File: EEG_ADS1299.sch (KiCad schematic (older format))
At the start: 68 parts, among them IC1 ADS1299, P1 CONN_2, P2 CONN_2, P3 CONN_01X06, U1 TPS61221, U2 TPS61222, U3 NRF528XX-QFAA, U4 MPU-9250, U5 INA828, U6 INA828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

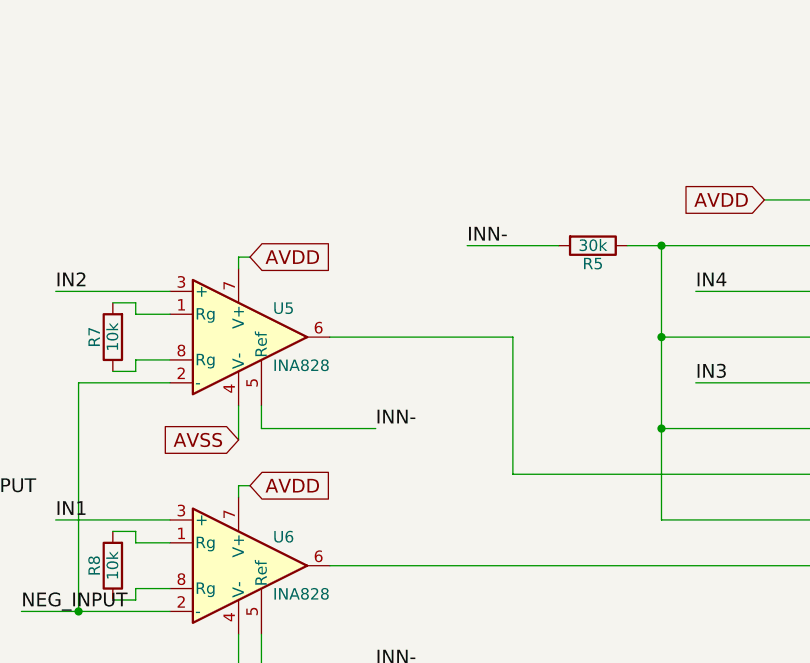
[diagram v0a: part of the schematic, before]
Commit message: (#1) - Added single capacitor on amp inputs. (C37)
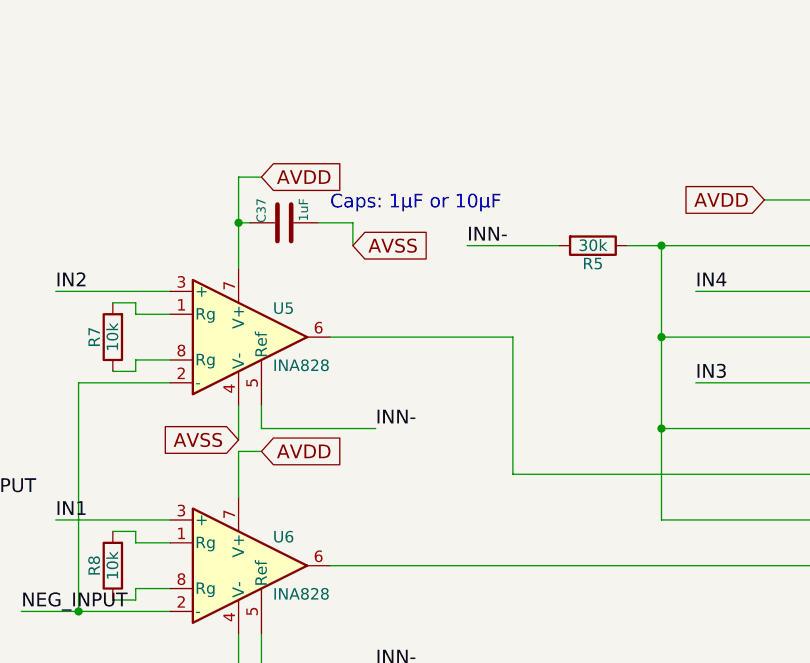
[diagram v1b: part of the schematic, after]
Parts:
- added C37: 1uF, Capacitors_SMD:C_0402, symbol C
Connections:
- wire segments 310 -> 313
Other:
- note added: "Caps: 1µF or 10µF"
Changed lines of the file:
@@
 Text GLabel 10600 11950 0    60   Input ~ 0
 AVSS
-Text GLabel 10650 11100 2    60   Input ~ 0
+Text GLabel 10700 10950 2    60   Input ~ 0
 AVDD
-Text GLabel 10650 10100 2    60   Input ~ 0
+Text GLabel 10700 9750 2    60   Input ~ 0
 AVDD
 $Comp
@@
 	10050 10600 10150 10600
 Wire Wire Line
-	10600 10100 10650 10100
-Wire Wire Line
-	10600 10150 10600 10100
-Wire Wire Line
-	10600 11100 10650 11100
-Wire Wire Line
-	10600 11100 10600 11150
+	10600 9750 10600 10150
+Wire Wire Line
+	10600 10950 10600 11150
 Wire Wire Line
 	10700 11900 11200 11900
@@
 Wire Wire Line
 	13850 10450 12450 10450
+$Comp
+L C C37
+U 1 1 5A28A53A
+P 10800 9950
+F 0 "C37" H 10800 10050 40  0000 L CNN
+F 1 "1uF" H 10806 9865 40  0000 L CNN
+F 2 "Capacitors_SMD:C_0402" H 10838 9800 30  0001 C CNN
+F 3 "~" H 10800 9950 60  0000 C CNN
+	1    10800 9950
+	0    -1   -1   0
+$EndComp
+Wire Wire Line
+	10600 9750 10700 9750
+Wire Wire Line
+	10600 9950 10650 9950
+Connection ~ 10600 9950
+Wire Wire Line
+	10950 9950 11100 9950
+Wire Wire Line
+	11100 9950 11100 10050
+Text GLabel 11100 10050 2    60   Input ~ 0
+AVSS
+Wire Wire Line
+	10600 10950 10700 10950
+Text Notes 11000 9900 0    60   ~ 0
+Caps: 1µF or 10µF
 $EndSCHEMATC

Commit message: Added TPS63001, TPS22941.
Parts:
- removed U1: TPS61221, TO_SOT_Packages_SMD:SOT-363_SC-70-6, symbol TPS61221
- added C38, C39: 10uF, Capacitors_SMD:C_0402, symbol C
- added C40: 1uF, Capacitors_SMD:C_0402, symbol C
- added R10, R9: 1M, Resistors_SMD:R_0402, symbol R
- added U1: TPS2294x, TO_SOT_Packages_SMD:SOT-353_SC-70-5, symbol TPS2294x
- added U7: TPS63001, Housings_DFN_QFN:DFN-10-1EP_3x3mm_Pitch0.5mm, symbol TPS63001
- L1: value 4.7µH -> 2.2µH
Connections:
- net labels added: AIN_BAT_DIV_VOLTAGE, IN1N, IN2N, IN3N, IN4N, LOAD_SW_CTRL, Vout
- net labels removed: BATT_ADC_AIN, BATT_VOLTAGE, GPIO_CTRL_PWR_ON, IN3-, IN4-
- wire segments 313 -> 348
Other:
- moved on the sheet: C1, C2, L1, P3

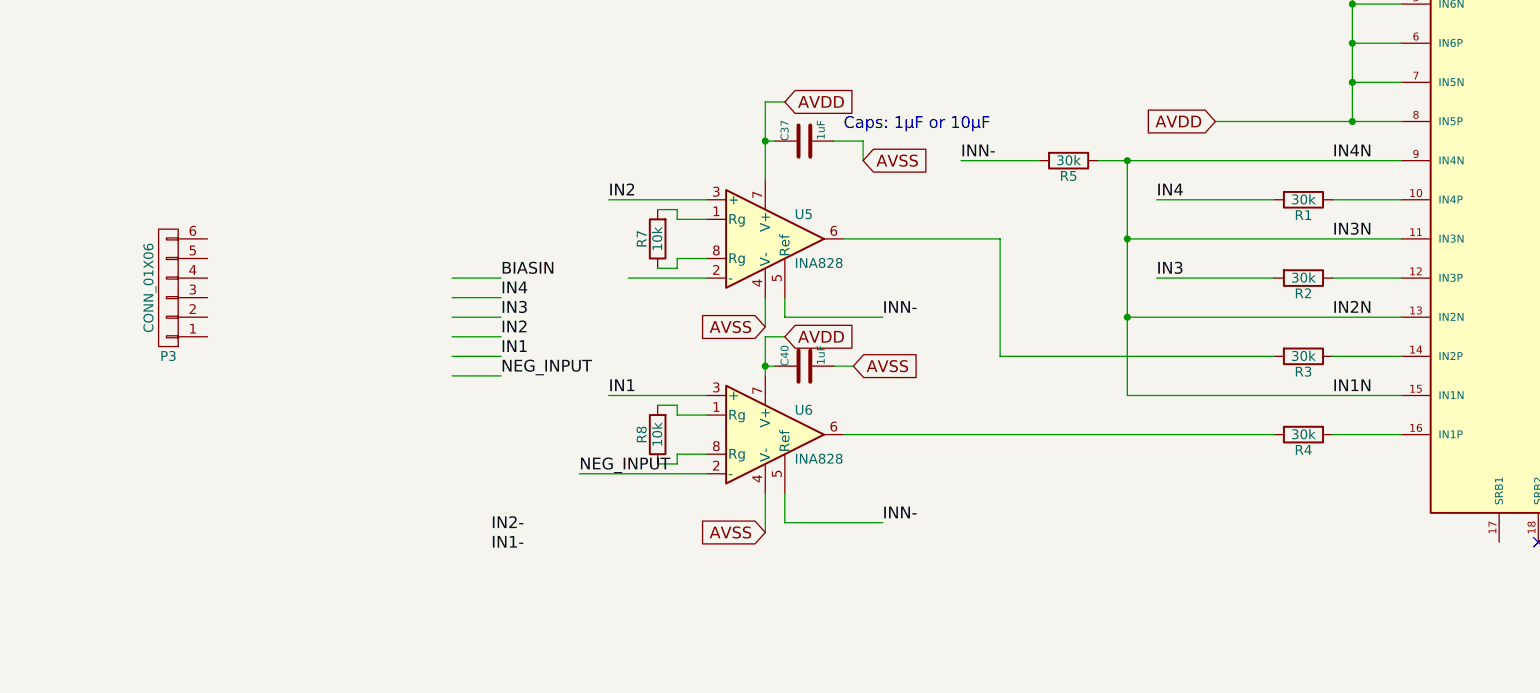
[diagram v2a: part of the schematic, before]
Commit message: Fixed design and separated channels 1 and 2 from 3 and 4, with 1 and 2 being the pre-amplified circuits.
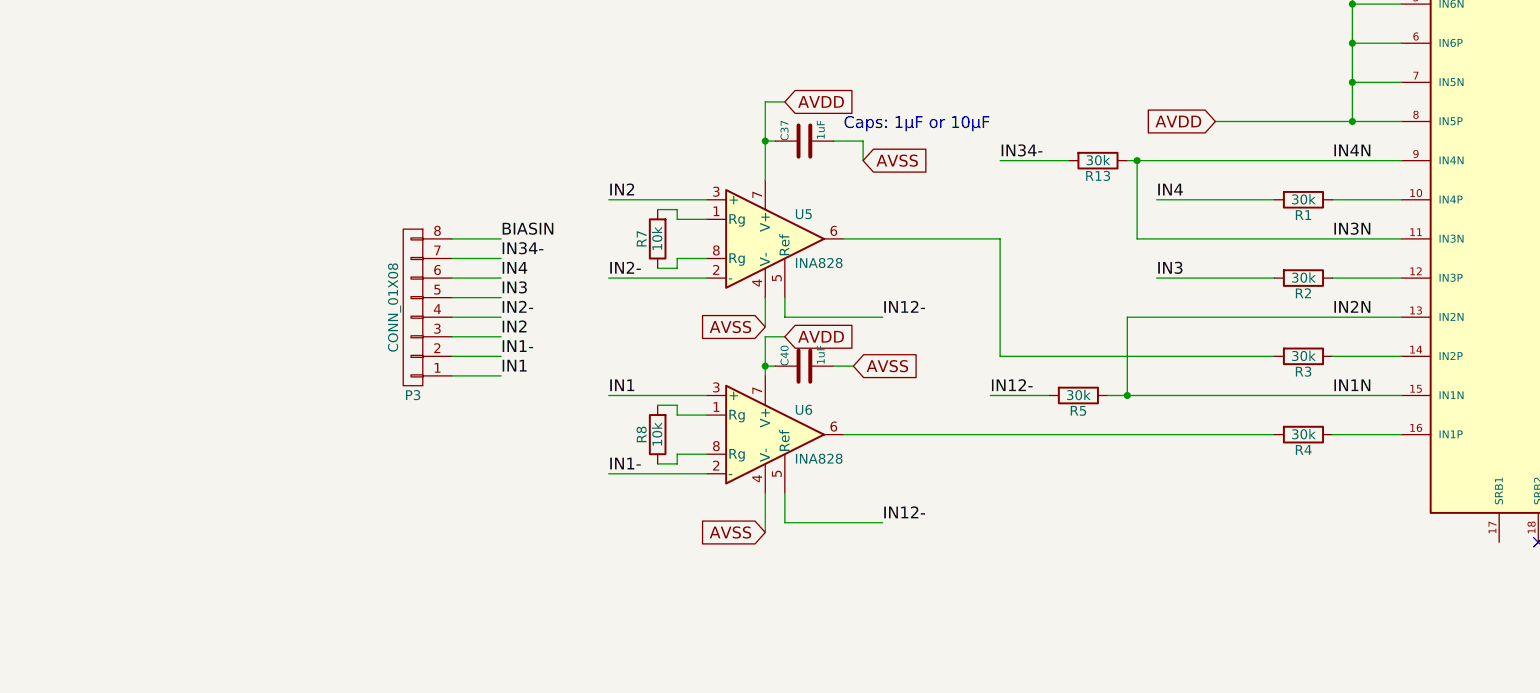
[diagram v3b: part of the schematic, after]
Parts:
- removed P3: CONN_01X06, Pin_Headers:Pin_Header_Straight_1x06_Pitch2.54mm, symbol CONN_01X06
- added P3: CONN_01X08, symbol CONN_01X08
- added R13: 30k, Resistors_SMD:R_0402, symbol R
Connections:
- net NEG_INPUT is gone; now on net IN1-: U6.2 (-)
- net BIASIN: now also P3.8 (P8)
- net IN1: now also P3.1 (P1)
- net IN1-: now also P3.2 (P2)
- net IN1N: no longer IC1.11 (IN3N), IC1.9 (IN4N)
- net IN2: now also P3.3 (P3)
- net IN2-: now also U5.2 (-), P3.4 (P4)
- net IN3: now also P3.5 (P5)
- net IN4: now also P3.6 (P6)
- net INN- renamed IN12-
- new net IN34-: P3.7 (P7), R13.2
- new net IN3N: IC1.11 (IN3N), IC1.9 (IN4N), R13.1
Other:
- moved on the sheet: R5
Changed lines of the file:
@@
 Text Label 13500 10050 0    60   ~ 0
 IN4N
-Text Label 9200 11950 0    60   ~ 0
+Text Label 9250 10850 0    60   ~ 0
 IN2-
-Text Label 9200 12050 0    60   ~ 0
+Text Label 9250 11050 0    60   ~ 0
 IN1-
 $Comp
@@
 L R R5
 U 1 1 5A25E958
-P 12150 10050
-F 0 "R5" V 12230 10050 50  0000 C CNN
-F 1 "30k" V 12150 10050 50  0000 C CNN
-F 2 "Resistors_SMD:R_0402" V 12080 10050 50  0001 C CNN
-F 3 "" H 12150 10050 50  0000 C CNN
-	1    12150 10050
+P 12200 11250
+F 0 "R5" V 12280 11250 50  0000 C CNN
+F 1 "30k" V 12200 11250 50  0000 C CNN
+F 2 "Resistors_SMD:R_0402" V 12130 11250 50  0001 C CNN
+F 3 "" H 12200 11250 50  0000 C CNN
+	1    12200 11250
 	0    1    1    0
 $EndComp
-Text Label 11600 10050 0    60   ~ 0
-INN-
+Text Label 11750 11250 0    60   ~ 0
+IN12-
 $Comp
 L INA128 U5
@@
 	1    0    0    -1
 $EndComp
-Text Label 11200 10850 0    60   ~ 0
-INN-
-Text Label 11200 11900 0    60   ~ 0
-INN-
 Text GLabel 10600 10900 0    60   Input ~ 0
 AVSS
@@
 Text Label 9800 10250 0    60   ~ 0
 IN2
-Text Label 9650 11650 0    60   ~ 0
-NEG_INPUT
-$Comp
-L CONN_01X06 P3
-U 1 1 5A2786C7
-P 7550 10700
-F 0 "P3" H 7550 11050 50  0000 C CNN
-F 1 "CONN_01X06" V 7650 10700 50  0000 C CNN
-F 2 "Pin_Headers:Pin_Header_Straight_1x06_Pitch2.54mm" H 7550 10700 50  0001 C CNN
-F 3 "" H 7550 10700 50  0001 C CNN
-	1    7550 10700
-	-1   0    0    1
-$EndComp
+Text Label 9250 10650 0    60   ~ 0
+IN4
 Text Label 9250 10750 0    60   ~ 0
-IN4
-Text Label 9250 10850 0    60   ~ 0
 IN3
 Text Label 9250 10950 0    60   ~ 0
 IN2
-Text Label 9250 11050 0    60   ~ 0
+Text Label 9250 11150 0    60   ~ 0
 IN1
-Text Label 9250 11150 0    60   ~ 0
-NEG_INPUT
-Text Label 9250 10650 0    60   ~ 0
+Text Label 9250 10450 0    60   ~ 0
 BIASIN
 Text Label 13500 10450 0    60   ~ 0
@@
 	11000 10450 11800 10450
 Wire Wire Line
-	9650 11650 10300 11650
-Wire Wire Line
 	10300 11250 9800 11250
 Wire Wire Line
@@
 Wire Wire Line
 	11000 11450 13200 11450
-Wire Wire Line
-	12000 10050 11600 10050
-Connection ~ 12450 10850
-Connection ~ 12450 10450
-Connection ~ 12450 10050
-Wire Wire Line
-	12450 10050 12450 11250
 Connection ~ 2450 6800
 Wire Wire Line
@@
 	25050 4400 26200 4400
 Wire Wire Line
-	12300 10050 13850 10050
-Wire Wire Line
-	12450 11250 13850 11250
+	12350 11250 13850 11250
 Wire Wire Line
 	12450 10850 13850 10850
@@
 	23800 5700 23800 6850
 Wire Wire Line
-	9900 10650 10300 10650
+	9800 10650 10300 10650
+Wire Wire Line
+	9000 10550 9250 10550
 Wire Wire Line
 	9000 10650 9250 10650
@@
 	9000 10850 9250 10850
 Wire Wire Line
-	9000 10950 9250 10950
-Wire Wire Line
 	9000 11050 9250 11050
 Wire Wire Line
 	9000 11150 9250 11150
-Wire Wire Line
-	13850 10450 12450 10450
 Wire Wire Line
 	10600 9750 10700 9750
@@
 Text Label 13500 10850 0    60   ~ 0
 IN2N
+Wire Wire Line
+	9000 10950 9250 10950
+Wire Wire Line
+	10300 11650 9800 11650
+Text Label 9800 11650 0    60   ~ 0
+IN1-
+Text Label 9800 10650 0    60   ~ 0
+IN2-
+Wire Wire Line
+	12450 11250 12450 10850
+Connection ~ 12450 11250
+Wire Wire Line
+	12050 11250 11750 11250
+Text Label 11800 10050 0    60   ~ 0
+IN34-
+Text Label 11200 10850 0    60   ~ 0
+IN12-
+Text Label 11200 11900 0    60   ~ 0
+IN12-
+Wire Wire Line
+	12500 10450 13850 10450
+$Comp
+L R R13
+U 1 1 5A31B95B
+P 12300 10050
+F 0 "R13" V 12380 10050 50  0000 C CNN
+F 1 "30k" V 12300 10050 50  0000 C CNN
+F 2 "Resistors_SMD:R_0402" V 12230 10050 50  0001 C CNN
+F 3 "" H 12300 10050 50  0000 C CNN
+	1    12300 10050
+	0    1    1    0
+$EndComp
+Wire Wire Line
+	12150 10050 11800 10050
+Wire Wire Line
+	12450 10050 13850 10050
+Wire Wire Line
+	12500 10050 12500 10450
+Connection ~ 12500 10050
+Wire Wire Line
+	9250 10450 9000 10450
+Text Label 9250 10550 0    60   ~ 0
+IN34-
+$Comp
+L CONN_01X08 P3
+U 1 1 5A321A4A
+P 8800 10800
+F 0 "P3" H 8800 11250 50  0000 C CNN
+F 1 "CONN_01X08" V 8900 10800 50  0000 C CNN
+F 2 "" H 8800 10800 50  0000 C CNN
+F 3 "" H 8800 10800 50  0000 C CNN
+	1    8800 10800
+	-1   0    0    1
+$EndComp
 $EndSCHEMATC
